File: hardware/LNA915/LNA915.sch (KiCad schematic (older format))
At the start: 10 parts

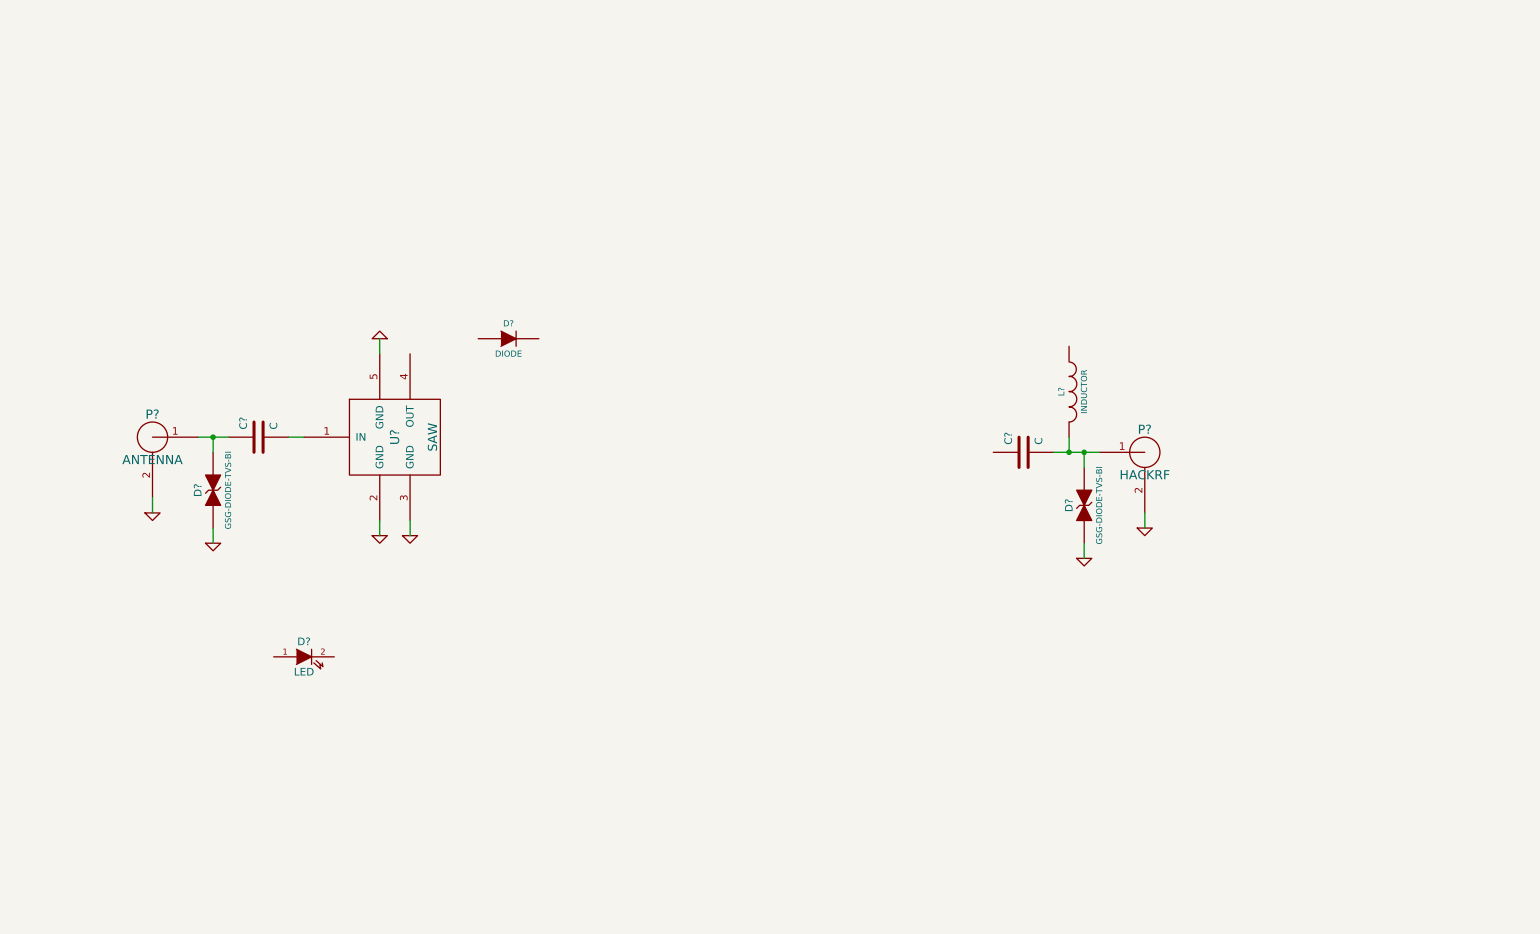
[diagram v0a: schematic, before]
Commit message: finished LNA915 schematic
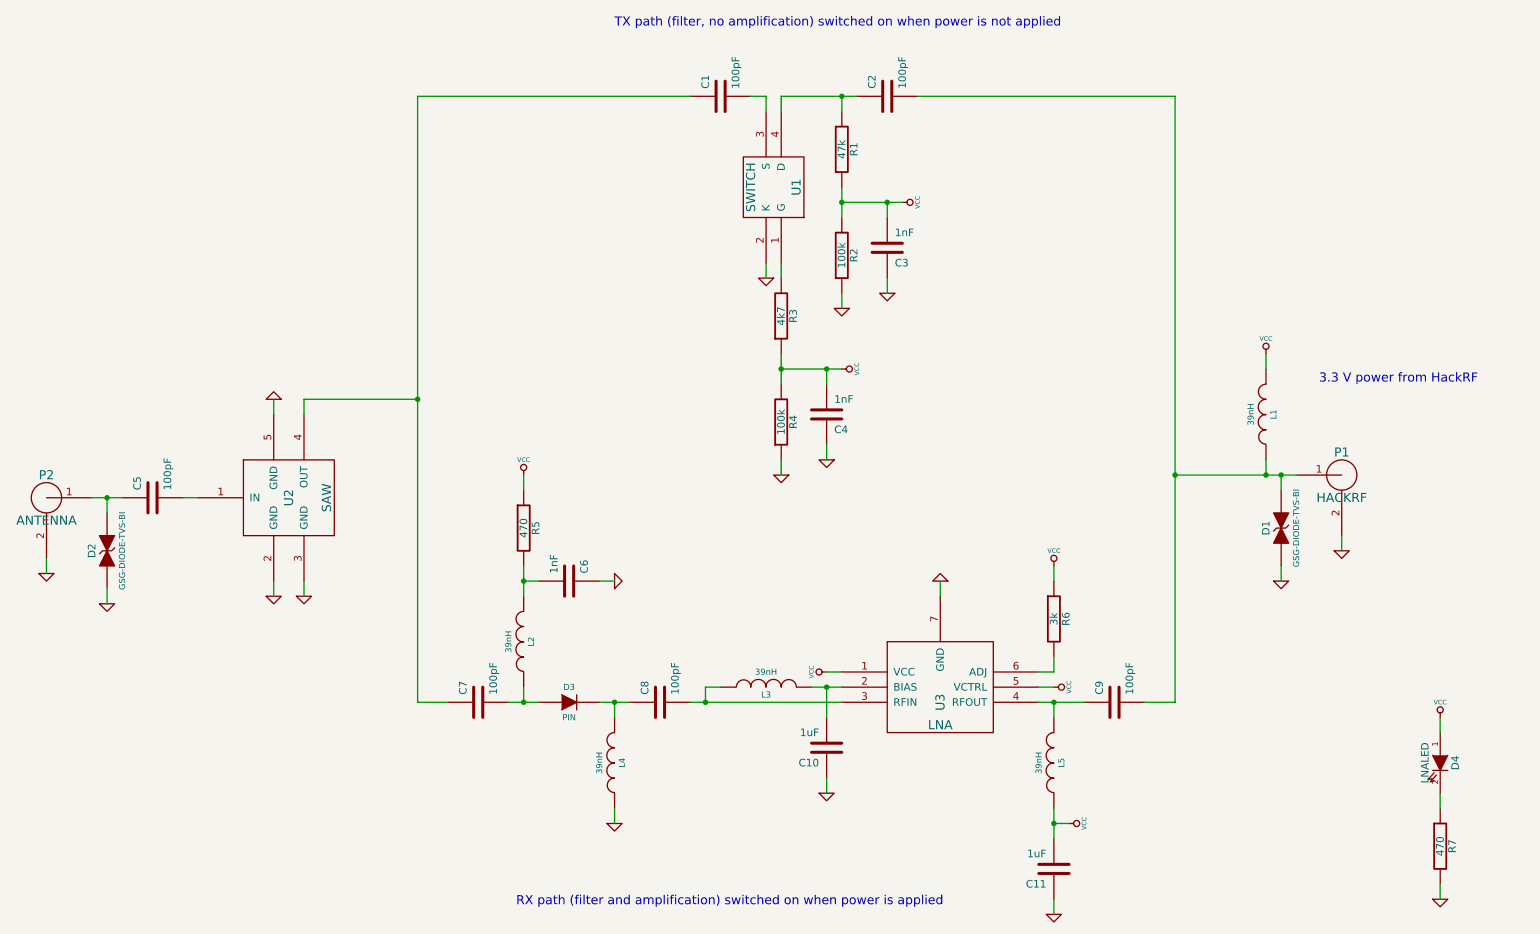
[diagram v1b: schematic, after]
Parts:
- removed C?: C, symbol C
- removed D?: GSG-DIODE-TVS-BI, ~, symbol GSG-DIODE-TVS-BI
- removed L?: INDUCTOR, symbol INDUCTOR
- removed P?: ANTENNA, ~, symbol GSG-RF-CONN
- added C1, C2, C7, C8, C9: 100pF, symbol C
- added C10, C11: 1uF, symbol C
- added C3, C4, C6: 1nF, symbol C
- added D2: GSG-DIODE-TVS-BI, ~, symbol GSG-DIODE-TVS-BI
- added L1, L2, L3, L4, L5: 39nH, symbol INDUCTOR
- added P2: ANTENNA, ~, symbol GSG-RF-CONN
- added R1: 47k, symbol R
- added R2, R4: 100k, symbol R
- added R3: 4k7, symbol R
- added R5, R7: 470, symbol R
- added R6: 3k, symbol R
- added U1: SWITCH, symbol BF1118
- added U3: LNA, ~, symbol BGB741L7ESD
- C5: renamed from C?; value C -> 100pF; Description (none) -> CAP CER 100PF 50V 5% NP0 0402; Manufacturer (none) -> Murata; Part Number (none) -> GRM1555C1H101JA01D
- D1: renamed from D?; Description (none) -> TVS DIODE ESD .05PF 15KV 0402; Manufacturer (none) -> Murata; Part Number (none) -> LXES15AAA1-100
- D3: renamed from D?; value DIODE -> PIN; Description (none) -> DIODE PIN GP 50V 100MA SOD323; Manufacturer (none) -> NXP; Part Number (none) -> BAP50-03
- D4: renamed from D?; value LED -> LNALED; Description (none) -> LED GREEN STD BRIGHT 0603 SMD; Manufacturer (none) -> Everlight; Part Number (none) -> QTLP601C4TR
- P1: renamed from P?; Description (none) -> CONN SMA JACK 50 OHM EDGE MNT; Manufacturer (none) -> Linx Technology; Part Number (none) -> CONSMA003.062
- gave numbers to parts that had none: 1
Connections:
- net GND: now also C10.1, C11.1, C3.1, C4.1, C6.1, D2.1 (A), L4.1, P2.2 (GND), R2.1, R4.1, R7.2, U1.2 (K), U3.7 (GND)
- net at D3.1 (A): now also C7.2, L2.1
- net at D3.2 (K): now also C8.1, L4.2
- net at C5.1: now also D2.2 (K), P2.1 (RF)
- net at D1.2 (K), P1.1 (RF): now also C2.2, C9.2, L1.1
- net at U2.4 (OUT): now also C1.1, C7.1
- net VCC: now reaches D4.1 (A)
- net VCC: now also C11.2, C3.2, C4.2, L1.2, L5.1, R1.1, R2.2, R3.1, R4.2, R5.1, R6.1, U3.1 (VCC), U3.5 (VCTRL)
- net at D4.2 (K): now also R7.1
- new net: C10.2, L3.2, U3.2 (BIAS)
- new net: C8.2, L3.1, U3.3 (RFIN)
- new net: C9.1, L5.2, U3.4 (RFOUT)
- new net: R6.2, U3.6 (ADJ)
- new net: R3.2, U1.1 (G)
- new net: C1.2, U1.3 (S)
- new net: C2.1, R1.2, U1.4 (D)
- new net: C6.2, L2.2, R5.2
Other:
- note added: "3.3 V power from HackRF"
- note added: "RX path (filter and amplification) switched on when power is applied\n"
- note added: "TX path (filter, no amplification) switched on when power is not applied"
- moved on the sheet: C5, D1, D3, D4, P1, U2
